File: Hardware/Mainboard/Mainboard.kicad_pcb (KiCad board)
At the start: 2 copper layers, 116.8 x 116.8 mm, 95 parts, among them J1 Conn_01x04_Pin, J2 USB_C_Receptacle_USB2.0_16P, Q1 Q_NMOS_GDS, Q2 Q_NMOS_GDS, SW1 SW_Push, SW2 SW_Push, U1 ESP32-S2-SOLO-2, U2 TLV62569DBV

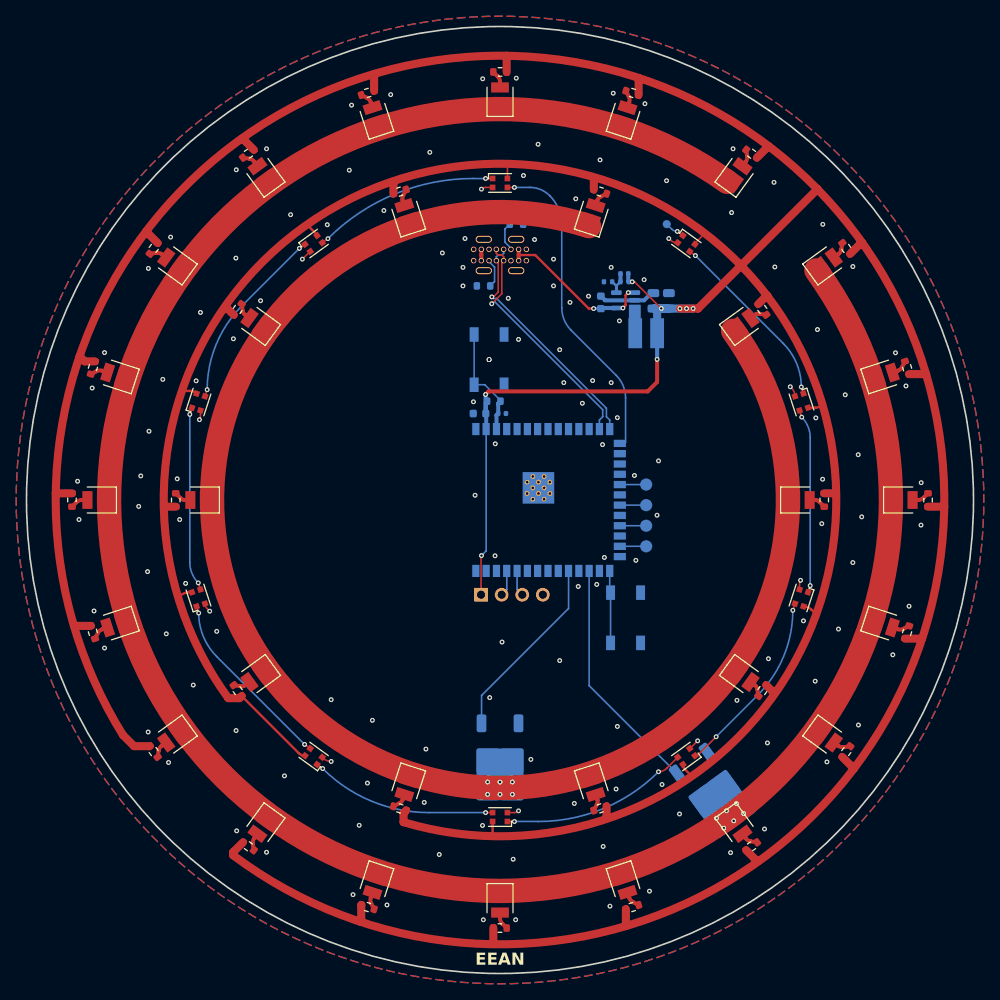
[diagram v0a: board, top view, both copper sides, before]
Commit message: Finalize layout, silkscreen, outline. Pending review
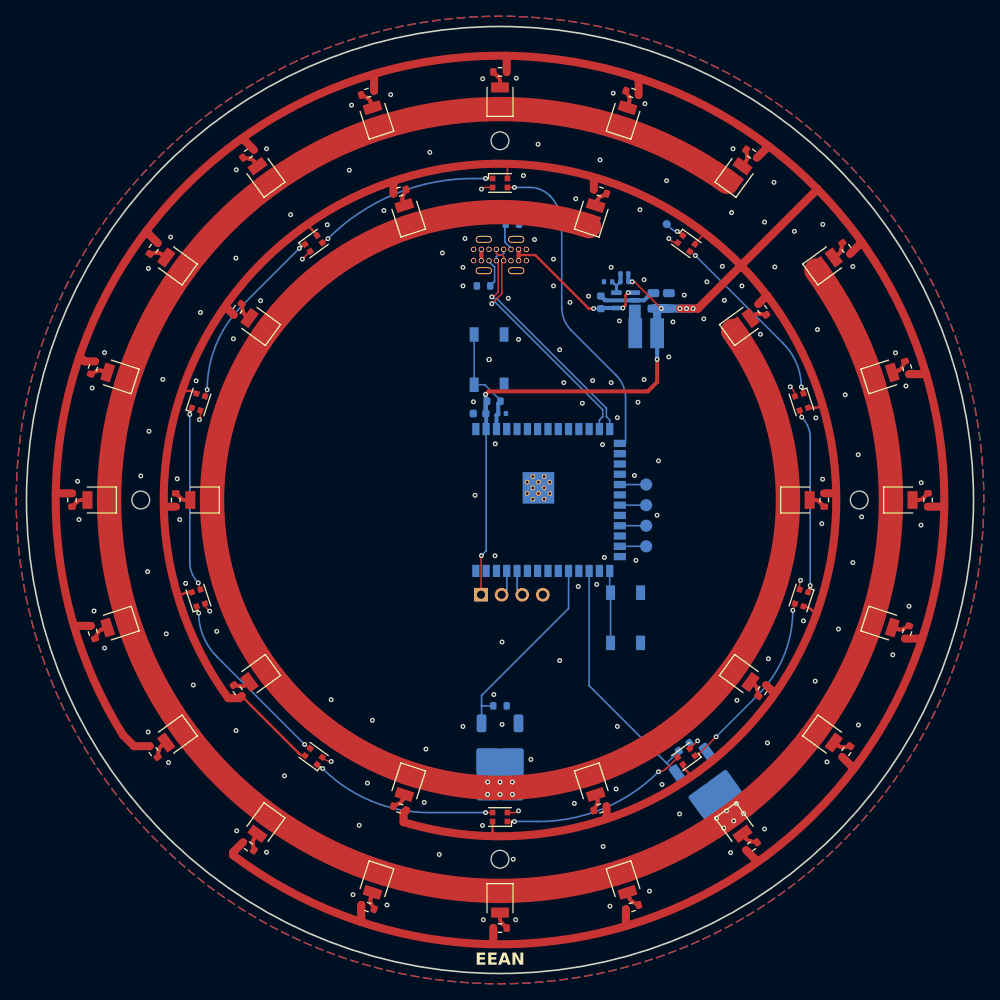
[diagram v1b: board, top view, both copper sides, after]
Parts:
- added R37: 100k, Resistor_SMD:R_0603_1608Metric, B.Cu at (127.0, 127.0)
- added R4: 100k, Resistor_SMD:R_0603_1608Metric, B.Cu at (149.7, 132.1)
- added REF**: MountingHole_2.2mm_M2, MountingHole:MountingHole_2.2mm_M2, F.Cu at (82.7, 101.6)
- added REF**: MountingHole_2.2mm_M2, MountingHole:MountingHole_2.2mm_M2, F.Cu at (171.3, 101.6)
- added REF**: MountingHole_2.2mm_M2, MountingHole:MountingHole_2.2mm_M2, F.Cu at (127.0, 145.9)
- added REF**: MountingHole_2.2mm_M2, MountingHole:MountingHole_2.2mm_M2, F.Cu at (127.0, 57.3)
- moved R2 0.51 mm to (128.5, 67.6)
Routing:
- net CTRL_3000k: track 29.5 -> 31.6 mm
- net CTRL_1800k: track 23.2 -> 24.7 mm
- net GND: vias 147 -> 163
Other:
- board text added: "BOOT"
- board text added: "IO11"
- board text added: "IO13"
- board text added: "IO21"
- board text added: "IO34"
- board text added: "RST"
- board text removed: "JLCJLCJLCJLC"
